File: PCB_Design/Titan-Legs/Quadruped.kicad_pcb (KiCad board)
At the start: 4 copper layers, 55.5 x 55.5 mm, 82 parts, among them IC1 TPS54260DGQR, IC2 CP2102, IC3 DRV8323RSRGZT, J1 TYPE-C-31-M-12, J2 1546216-3, P1 282837-2, P2 282837-2, Q1 BSC031N06NS3GATMA1, Q2 BSC031N06NS3GATMA1, Q3 BSC031N06NS3GATMA1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

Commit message: updating recent changes
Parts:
- added G***: LOGO, Logos:sralogo, B.Cu at (57.2, 86.9)
- added R10: 4.7K, Resistor_SMD:R_0603_1608Metric, F.Cu at (30.5, 114.6)
- added U5: DS18S20Z+, Temp-Sensor_DS18S20Z_:DS18S20Z_, F.Cu at (34.1, 114.1)
- C8: moved to B.Cu
- D1, D_Zener1: footprint SS34_NEW:DIOM8059X256N -> Diode_SMD:D_SMB
- J2: value 1546216-3 -> 691214110003; footprint TB - 3:15462163 -> TerminalBlock:TerminalBlock_bornier-3_P5.08mm
- moved R23 55.1 mm to (54.4, 112.6), turned to 90 degrees
- moved C29 53.0 mm to (52.7, 112.6), turned to 90 degrees
- moved C9 50.1 mm to (72.6, 116.1)
- moved C28 46.1 mm to (71.1, 112.8), turned to 180 degrees
- moved U2 45.0 mm to (56.5, 103.1)
- moved R24 43.8 mm to (54.4, 115.7), turned to -90 degrees
- moved C27 40.9 mm to (71.1, 114.3), turned to 180 degrees
- moved C10 40.2 mm to (48.5, 85.8)
- moved C4 40.0 mm to (62.4, 116.2), turned to 90 degrees
- moved C8 39.3 mm to (56.6, 108.8), turned to -90 degrees
- moved C31 38.5 mm to (59.4, 109.8)
- moved C7 38.0 mm to (68.0, 112.2)
- moved R12 37.8 mm to (67.6, 97.8), turned to 180 degrees
- moved C3 36.9 mm to (56.1, 115.7), turned to -90 degrees
- moved C11 36.5 mm to (51.6, 85.8)
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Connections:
- net /DC2 renamed /D-
- net /DC3 renamed /D+
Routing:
- net GND: track 72.2 -> 193.3 mm, vias 0 -> 2
- net 3V3_IN: track 99.2 -> 22.3 mm, vias 6 -> 0
- net Net-(C31-Pad2): track 0.00 -> 23.4 mm, vias 0 -> 2
- net /IO17: track 0.00 -> 21.1 mm
- net /IO18: track 0.00 -> 18.7 mm, vias 0 -> 2
- net /DRV8323/GHC: track 0.00 -> 18.0 mm, vias 0 -> 2
- net /IO11: track 0.00 -> 15.9 mm, vias 0 -> 1
- net /ESP_3V3: track 8.65 -> 23.0 mm, vias 0 -> 2
- net /IO13: track 0.00 -> 13.7 mm, vias 0 -> 1
- net /IO14: track 0.00 -> 13.2 mm, vias 0 -> 1
- net Net-(C29-Pad1): track 0.00 -> 12.6 mm, vias 0 -> 2
- net Net-(J1-PadB5): track 0.00 -> 11.5 mm, vias 0 -> 2
- net Net-(J1-PadA5): track 0.00 -> 10.4 mm, vias 0 -> 2
- net /IO9: track 0.00 -> 10.4 mm, vias 0 -> 1
- net /D+: track 25.8 -> 17.1 mm
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- added copper zone on F.Cu, net /DRV8323/SPB
- added copper zone on F.Cu, net /DRV8323/SPC
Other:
- outline, holes or cut-outs redrawn
- board text added: "Designed by"
- board text added: "RAJ GUPTA & PRATHAM DESHMUKH"

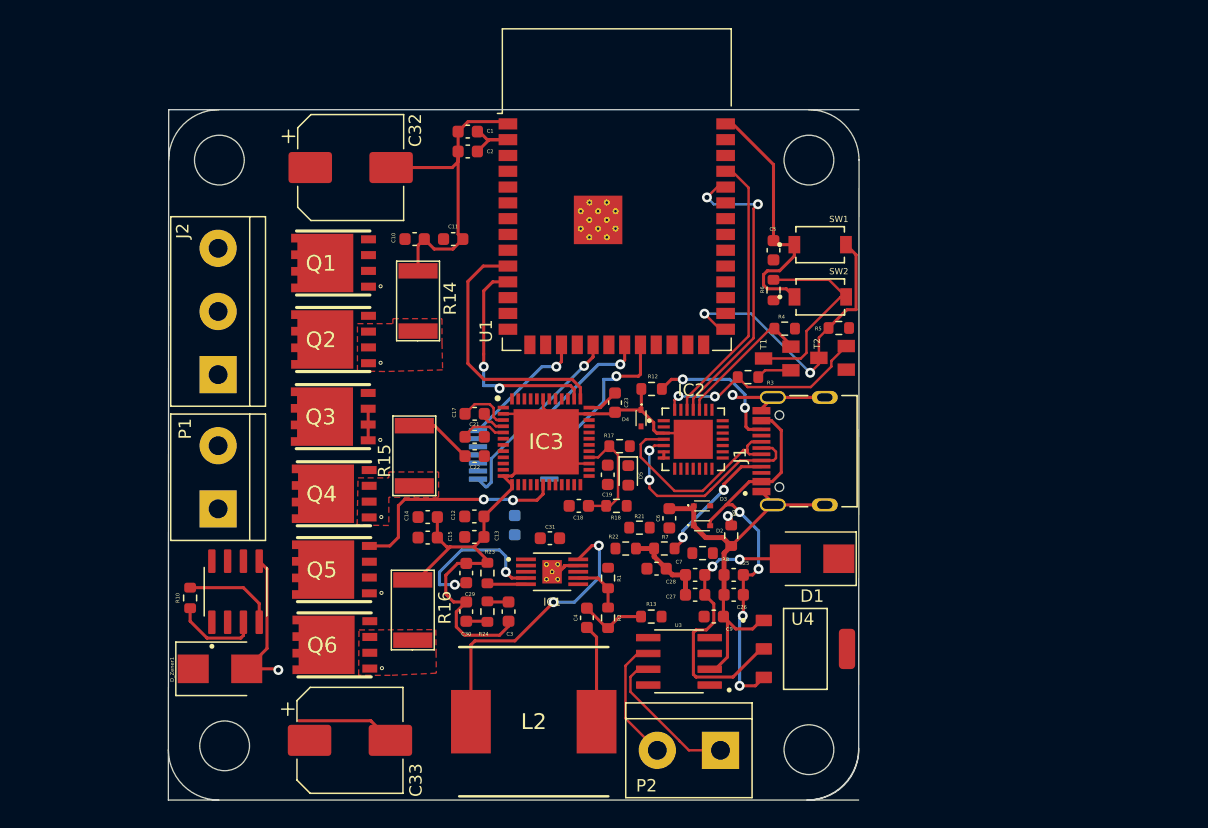
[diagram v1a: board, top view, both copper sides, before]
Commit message: Copper filled VM to mosfets
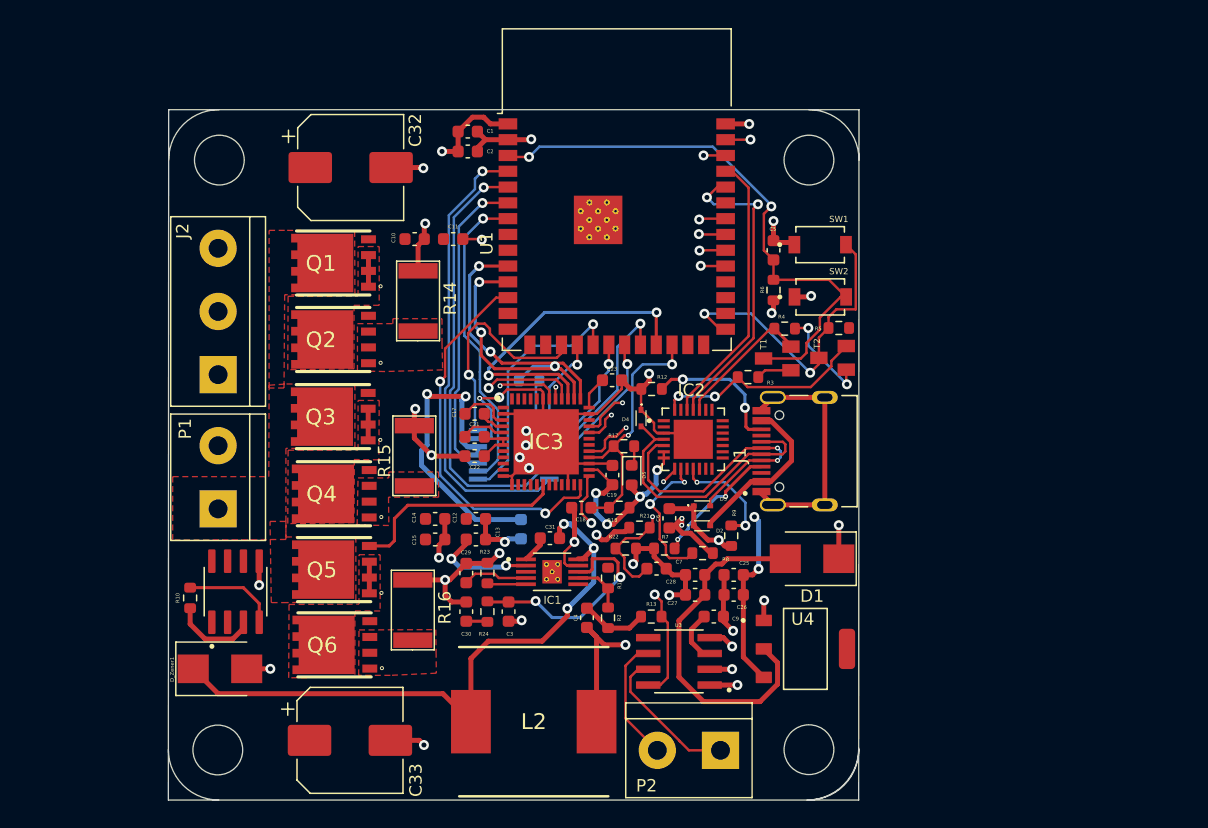
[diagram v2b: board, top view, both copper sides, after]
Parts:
- added R11: 10K, Resistor_SMD:R_0603_1608Metric, B.Cu at (57.8, 97.1)
- moved C23 1.82 mm to (64.4, 97.1), turned to 0 degrees
- moved H1 0.64 mm to (32.7, 126.8)
- moved C14 0.62 mm to (50.2, 108.2)
- moved C15 0.62 mm to (50.2, 109.9)
- moved C8 0.60 mm to (57.1, 109.1)
- moved C19 0.38 mm to (64.5, 104.7)
- moved R17 0.35 mm to (65.4, 102.4)
- moved D5 0.28 mm to (66.0, 104.7)
- moved R18 0.27 mm to (65.0, 107.3)
- moved C18 0.25 mm to (62.0, 107.3)
- moved C12 0.24 mm to (53.5, 108.2)
- moved C13 0.24 mm to (53.5, 109.9)
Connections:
- IC3 pad 37: /IO17 -> 3V3_IN
- IC3 pad 38: /IO18 -> 3V3_IN
- IC3 pad 41: /IO40 -> 3V3_IN
- U1 pad 10: /IO17 -> 3V3_IN
- U1 pad 11: /IO18 -> 3V3_IN
- U1 pad 33: /IO40 -> 3V3_IN
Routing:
- net 3V3_IN: track 22.3 -> 169.8 mm, vias 0 -> 18
- net Net-(C7-Pad1): track 0.00 -> 59.4 mm, vias 0 -> 4
- net /IO4: track 0.00 -> 36.8 mm, vias 0 -> 1
- net /IO2: track 0.00 -> 36.7 mm, vias 0 -> 2
- net /IO5: track 0.00 -> 34.7 mm, vias 0 -> 1
- net /IO39: track 0.00 -> 32.4 mm, vias 0 -> 2
- net /IO8: track 0.00 -> 31.1 mm, vias 0 -> 2
- net /EN: track 16.1 -> 46.2 mm, vias 0 -> 2
- net /IO41: track 0.00 -> 28.9 mm, vias 0 -> 2
- net Net-(C31-Pad2): track 23.4 -> 50.8 mm, vias 2 -> 3
- net /IO21: track 0.00 -> 26.5 mm, vias 0 -> 2
- net /IO7: track 0.00 -> 25.1 mm, vias 0 -> 1
- net /IO6: track 0.00 -> 25.0 mm, vias 0 -> 1
- net /IO38: track 0.00 -> 21.6 mm, vias 0 -> 2
- net /IO17: track 21.1 -> 2.23 mm, vias 0 -> 1
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- added copper zone on F.Cu, net /DRV8323/MOTOR_A
- added copper zone on In1.Cu, net /DRV8323/MOTOR_A
- added copper zone on F.Cu, net /DRV8323/MOTOR_B
- added copper zone on F.Cu, net /DRV8323/MOTOR_C
- added copper zone on In1.Cu, net 3V3_IN
- added copper zone on In2.Cu, net GND
- added copper zone on F.Cu, net VM
- added copper zone on In1.Cu, net VM

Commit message: gpio pins updated
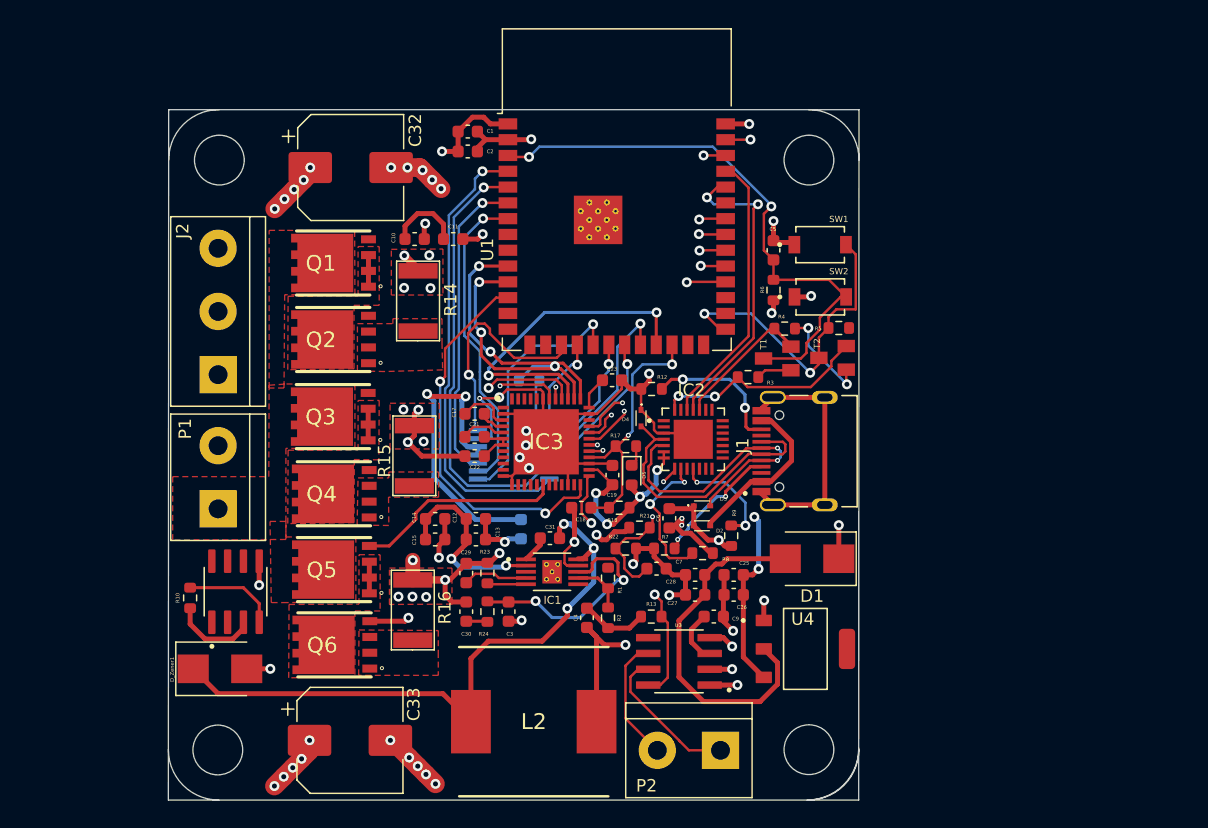
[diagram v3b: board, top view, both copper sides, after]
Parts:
- moved R17 0.16 mm to (65.5, 102.4)
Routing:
- net VM: track 12.4 -> 35.2 mm, vias 2 -> 12
- net /IO37: track 0.00 -> 21.8 mm, vias 0 -> 2
- net GND: track 178.1 -> 184.0 mm, vias 31 -> 49
- net /IO48: track 0.00 -> 3.90 mm, vias 0 -> 1
- net /DRV8323/GLC: track 0.00 -> 3.22 mm, vias 0 -> 1
- net /DRV8323/GHC: track 17.5 -> 16.7 mm
- added copper zone on F.Cu, net GND

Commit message: Add new placement for Quadruped PCB
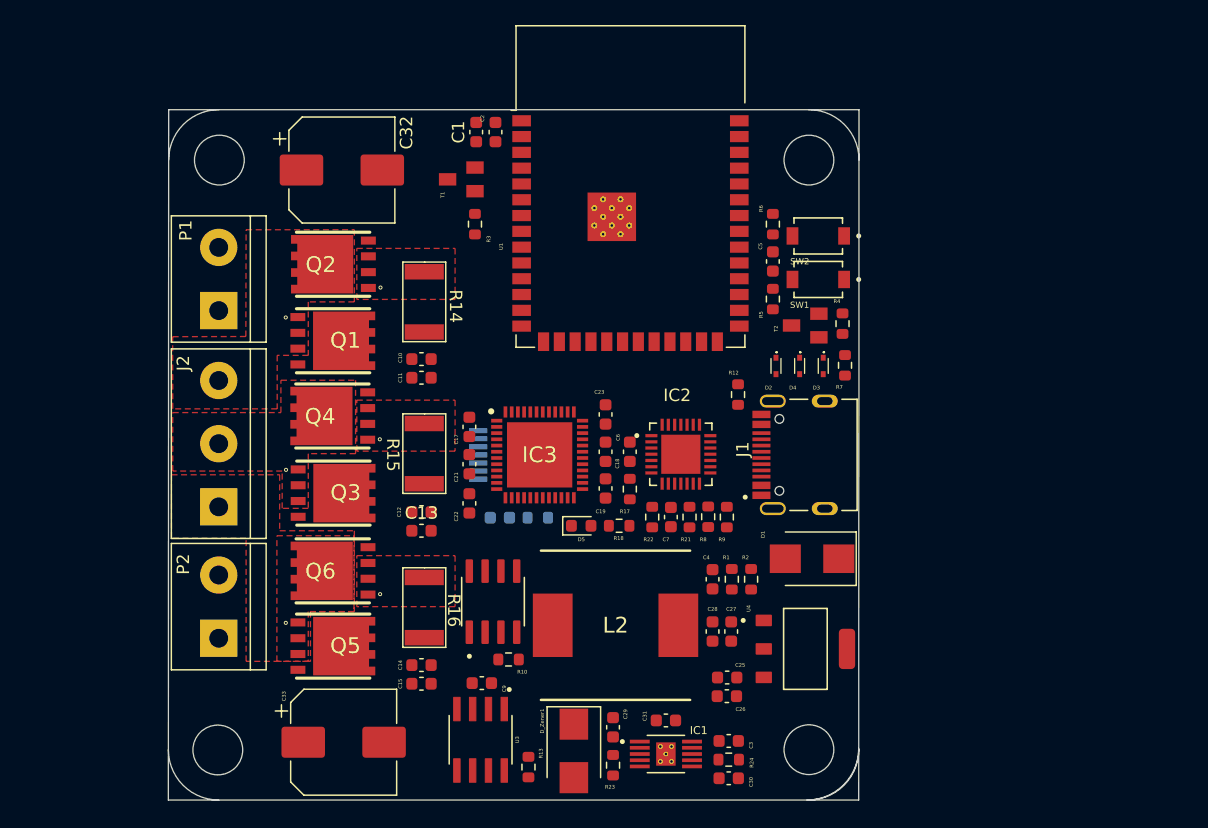
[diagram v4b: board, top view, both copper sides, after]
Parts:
- removed G***: LOGO, Logos:sralogo
- D2, D3, D4: footprint LESD_diode:LESD5D50CT1G -> diodes_USB-UART:LESD5D50CT1G
- IC3: footprint KiCad:QFN50P700X700X100-49N-D -> DRV8323RS:QFN50P700X700X100-49N-D
- moved P2 41.3 mm to (32.8, 117.8), turned to 90 degrees
- moved D_Zener1 29.2 mm to (61.4, 126.9), turned to -90 degrees
- moved T1 29.2 mm to (52.3, 81.0)
- moved R10 26.1 mm to (56.1, 119.5), turned to 0 degrees
- moved R3 25.2 mm to (53.4, 84.5), turned to 90 degrees
- moved C30 25.0 mm to (73.8, 129.1), turned to 180 degrees
- moved R24 22.8 mm to (73.8, 127.6), turned to 0 degrees
- moved U5 20.7 mm to (54.9, 114.9)
- moved R7 20.7 mm to (83.2, 95.9), turned to -90 degrees
- moved C3 20.5 mm to (73.8, 126.1), turned to 0 degrees
- moved C9 19.4 mm to (54.0, 121.5)
- moved R23 18.5 mm to (64.5, 128.1), turned to -90 degrees
- moved C31 17.4 mm to (68.8, 124.5)
- moved IC1 17.3 mm to (68.8, 127.2)
- moved U3 17.2 mm to (53.9, 126.0), turned to -90 degrees
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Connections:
- IC3 pad 37: 3V3_IN -> /IO15
- IC3 pad 38: 3V3_IN -> /IO16
- IC3 pad 41: 3V3_IN -> /IO40
- J2 pad 1: /DRV8323/MOTOR_A -> /DRV8323/MOTOR_C
- J2 pad 3: /DRV8323/MOTOR_C -> /DRV8323/MOTOR_A
- R10 pad 2: Net-(R10-Pad2) -> /IO20
- U1 pad 10: 3V3_IN -> /IO17
- U1 pad 11: 3V3_IN -> /IO18
- U1 pad 14: unconnected-(U1-Pad14) -> /IO20
- U1 pad 33: 3V3_IN -> /IO40
- U1 pad 8: unconnected-(U1-Pad8) -> /IO15
- U1 pad 9: unconnected-(U1-Pad9) -> /IO16
- U5 pad 4: Net-(R10-Pad2) -> /IO20
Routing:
- net GND: track 184.0 -> 0.12 mm, vias 49 -> 0
- net 3V3_IN: track 169.4 -> 0.00 mm, vias 18 -> 0
- net Net-(C7-Pad1): track 59.4 -> 0.00 mm, vias 4 -> 0
- net Net-(C31-Pad2): track 50.8 -> 0.00 mm, vias 3 -> 0
- net /EN: track 46.2 -> 0.00 mm, vias 2 -> 0
- net VBUS: track 45.7 -> 0.00 mm, vias 3 -> 0
- net /IO4: track 36.8 -> 0.00 mm, vias 1 -> 0
- net /IO2: track 36.7 -> 0.00 mm, vias 2 -> 0
- net VM: track 35.2 -> 0.00 mm, vias 12 -> 0
- net /IO5: track 34.7 -> 0.00 mm, vias 1 -> 0
- net /IO39: track 32.4 -> 0.00 mm, vias 2 -> 0
- net /IO8: track 31.1 -> 0.00 mm, vias 2 -> 0
- net /IO41: track 28.9 -> 0.00 mm, vias 2 -> 0
- net /ESP_3V3: track 28.7 -> 0.00 mm
- net /IO21: track 26.5 -> 0.00 mm, vias 2 -> 0
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- removed copper zone on In1.Cu, net /DRV8323/MOTOR_A
- removed copper zone on F.Cu, net GND
- removed copper zone on F.Cu, net VM
- removed copper zone on In1.Cu, net VM
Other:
- board text removed: "Designed by"
- board text removed: "RAJ GUPTA & PRATHAM DESHMUKH"

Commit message: Added high voltage copper fills
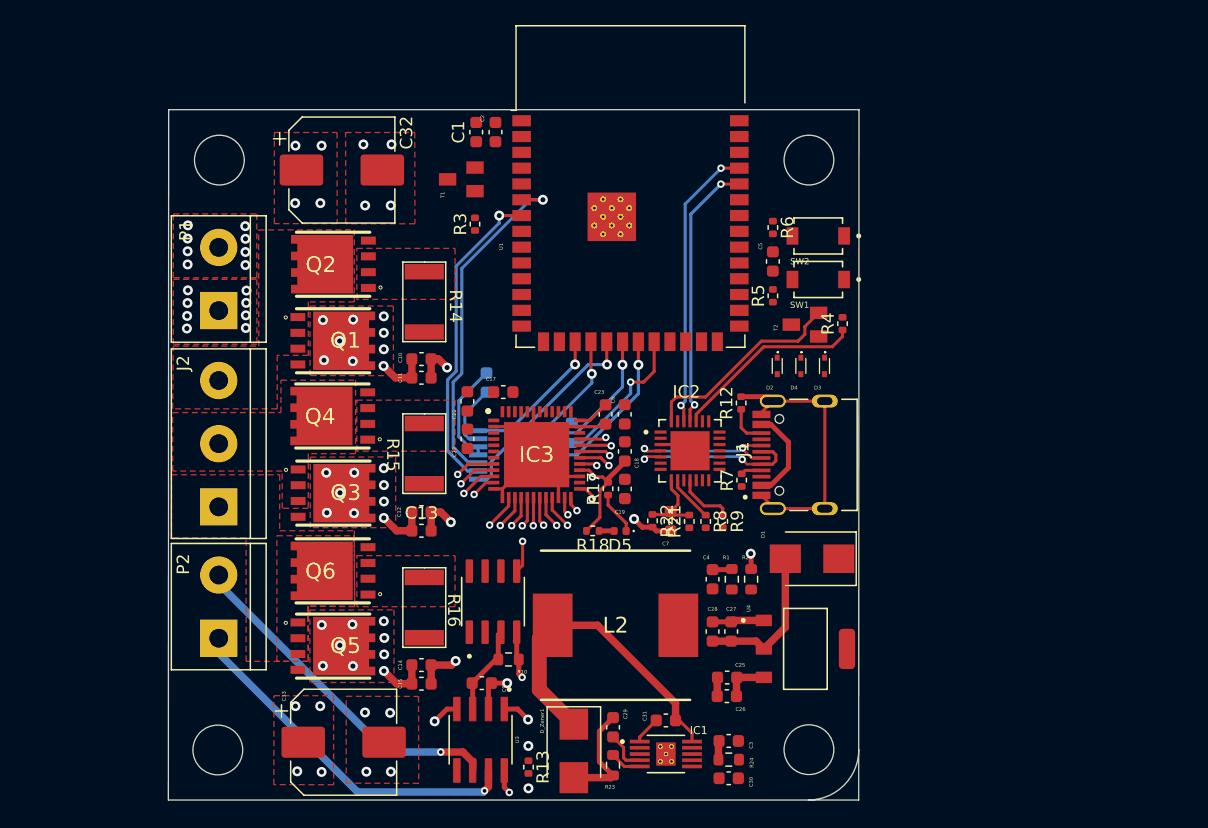
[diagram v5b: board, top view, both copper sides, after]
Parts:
- D5: footprint LED_SMD:LED_0603_1608Metric -> LED_SMD:LED_0402_1005Metric
- R12, R13, R17, R18, R21, R22, R3, R4, R5, R6, R7, R8, R9: footprint Resistor_SMD:R_0603_1608Metric -> Resistor_SMD:R_0402_1005Metric
- moved R7 12.4 mm to (74.8, 105.1), turned to 90 degrees
- moved C8 10.9 mm to (54.3, 97.3), turned to -90 degrees
- moved R11 7.36 mm to (61.2, 101.3), turned to -90 degrees
- moved C22 5.19 mm to (52.8, 101.8)
- moved C21 5.05 mm to (52.8, 98.8)
- moved C17 3.91 mm to (55.7, 98.0), turned to 180 degrees
- moved D5 3.16 mm to (65.1, 109.2), turned to 180 degrees
- moved C6 3.04 mm to (65.4, 99.8)
- moved R18 2.16 mm to (62.9, 109.2), turned to 180 degrees
- moved R17 1.75 mm to (64.1, 105.8)
- moved C19 1.55 mm to (65.5, 105.8)
- moved C18 1.55 mm to (65.5, 102.8)
- moved IC2 0.79 mm to (70.7, 102.8)
- moved R12 0.72 mm to (74.8, 98.9)
- moved R9 0.47 mm to (73.3, 108.4)
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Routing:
- net GND: track 0.12 -> 91.5 mm, vias 0 -> 24
- net /CAN_BUS_IC/CANH: track 0.00 -> 29.0 mm, vias 0 -> 1
- net /CAN_BUS_IC/CANL: track 0.00 -> 27.7 mm, vias 0 -> 1
- net /IO6: track 0.00 -> 27.7 mm, vias 0 -> 1
- net Net-(C31-Pad2): track 0.00 -> 25.8 mm
- net /IO7: track 0.00 -> 25.6 mm, vias 0 -> 1
- net /TXD: track 0.00 -> 23.2 mm, vias 0 -> 2
- net /RXD: track 0.00 -> 21.8 mm, vias 0 -> 2
- net 3V3_IN: track 0.00 -> 18.6 mm
- net /DTR: track 0.00 -> 16.7 mm
- net /IO11: track 0.00 -> 16.7 mm, vias 0 -> 1
- net /RTS: track 0.00 -> 15.4 mm
- net /D-: track 0.00 -> 14.1 mm, vias 0 -> 2
- net /IO14: track 0.00 -> 13.9 mm, vias 0 -> 1
- net /IO13: track 0.00 -> 13.4 mm, vias 0 -> 1
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- added copper zone on F.Cu, net GND
- added copper zone on F.Cu, net VM
- added copper zone on In1.Cu, net VM
- removed copper zone on In1.Cu, net 3V3_IN
- removed copper zone on In2.Cu, net GND
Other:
- outline, holes or cut-outs redrawn
